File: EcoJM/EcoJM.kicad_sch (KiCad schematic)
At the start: 50 parts, among them J1 Conn_01x01_Pin, J10 Conn_01x01_Pin, J11 Conn_01x01_Pin, J2 Conn_01x01_Pin, J3 Conn_01x02_Pin, J4 Conn_01x02_Pin, J5 Conn_01x03_Pin, J6 Conn_01x02_Pin, J7 Conn_01x03_Pin, J8 Screw_Terminal_01x02, J9 Screw_Terminal_01x02, Q1 2SD882_C842818, Q2 2SD882_C842818, U1 ACS712xLCTR-30A, U2 MT2492, U3 SIT65HVD230DR, U4 AZ1117-3.3, U5 RS321BXF, U6 STM32F_dev, U7 PC817C_C3025164, U8 PC817C_C3025164

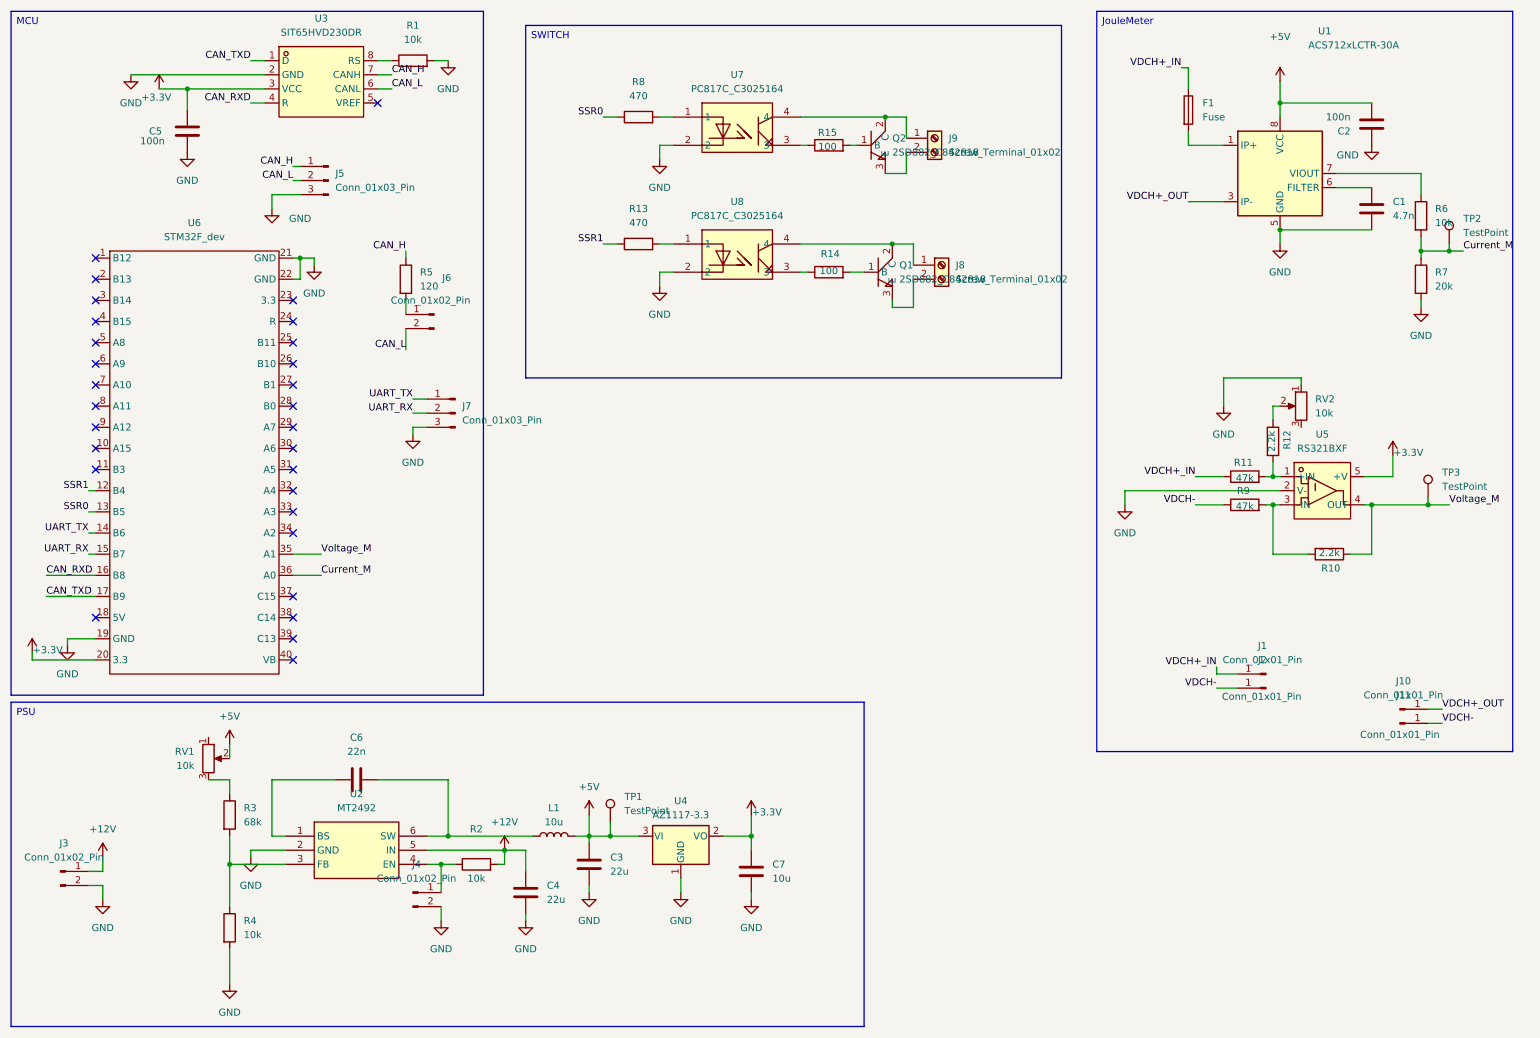
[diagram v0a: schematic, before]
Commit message: diff amp removed + potentiometer removed +SD card schematic done
diff amp removed + potentiometer removed +SD card schematic done
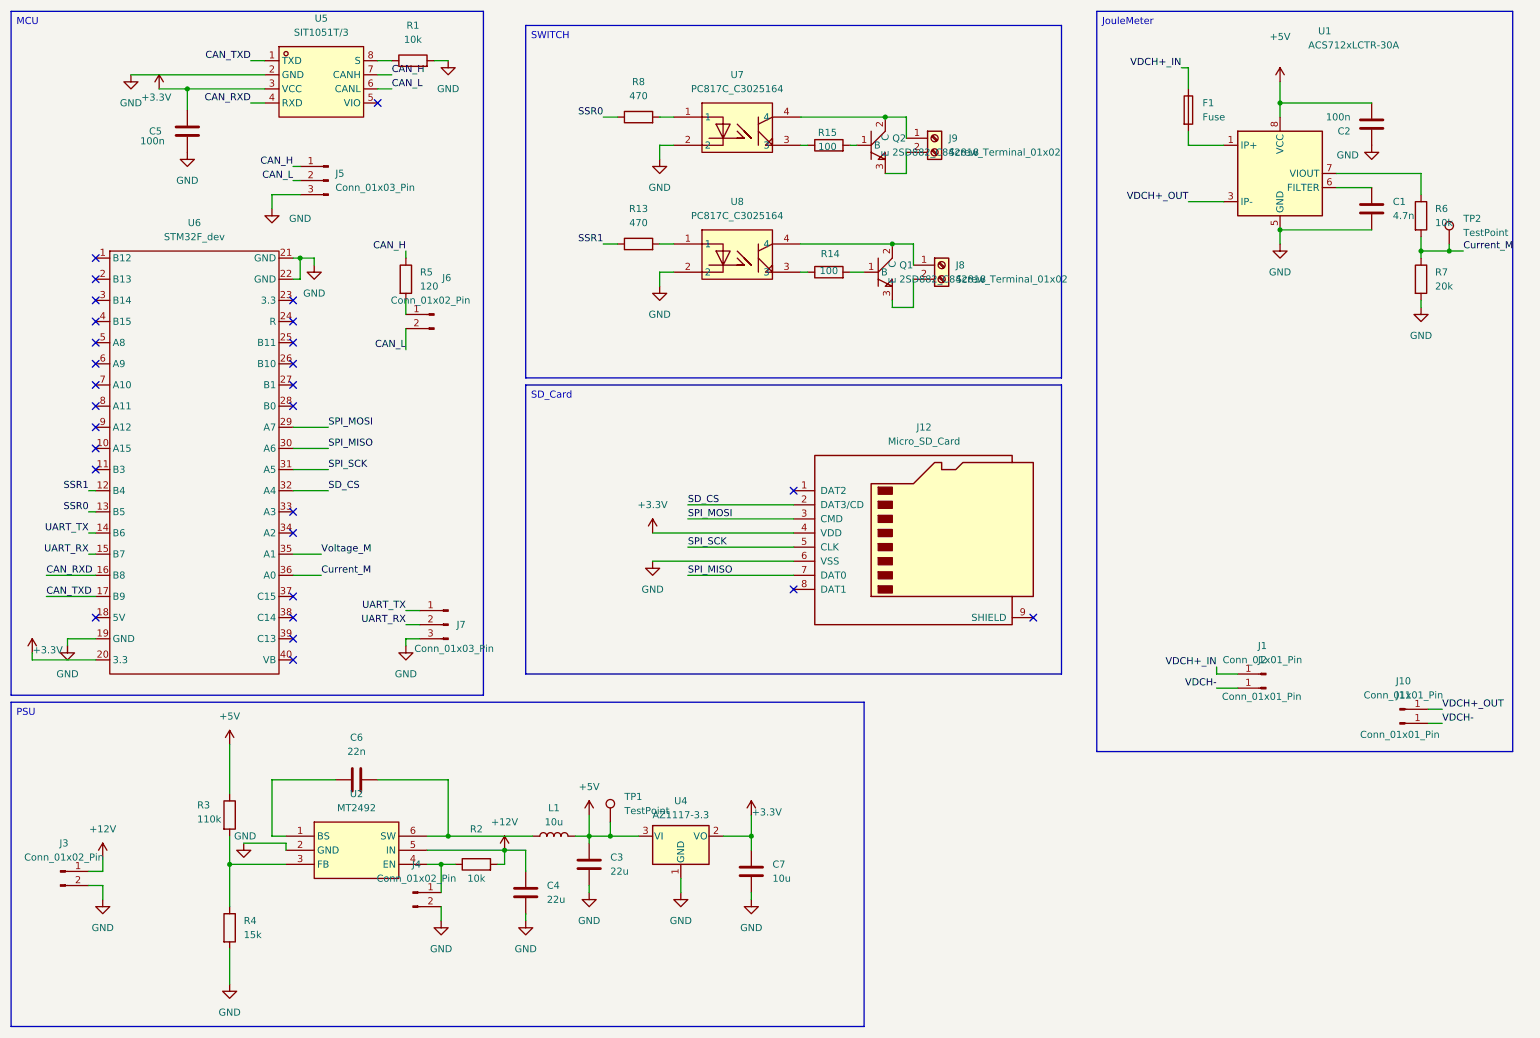
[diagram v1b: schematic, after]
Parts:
- removed R10, R12: 2.2k, Resistor_SMD:R_1206_3216Metric_Pad1.30x1.75mm_HandSolder, symbol Device:R
- removed R11, R9: 47k, Resistor_SMD:R_1206_3216Metric_Pad1.30x1.75mm_HandSolder, symbol Device:R
- removed RV1, RV2: 10k, Potentiometer_THT:Potentiometer_Bourns_3296W_Vertical, symbol Device:R_Potentiometer
- removed TP3: TestPoint, TestPoint:TestPoint_Pad_D1.5mm, symbol Connector:TestPoint
- removed U3: SIT65HVD230DR, EasyEDA:SOP-8_L4.9-W3.9-P1.27-LS6.0-BL, symbol EasyEDA:SIT65HVD230DR
- removed U5: RS321BXF, EasyEDA:SOT-23-5_L2.9-W1.6-P0.95-LS2.8-BL, symbol EasyEDA:RS321BXF
- added J12: Micro_SD_Card, symbol Connector:Micro_SD_Card
- added U5: SIT1051T/3, EasyEDA:SOP-8_L4.9-W3.9-P1.27-LS6.0-BL, symbol EasyEDAA:SIT1051T_3
- R3: value 68k -> 110k
- R4: value 10k -> 15k
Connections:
- net +3.3V: now also J12.4 (VDD), U5.3 (VCC)
- net +5V: now also R3.1
- net CAN_H: now also U5.7 (CANH)
- net CAN_L: now also U5.6 (CANL)
- net CAN_RXD: now also U5.4 (RXD)
- net CAN_TXD: now also U5.1 (TXD)
- net GND: now also J12.6 (VSS), U5.2 (GND)
- net at R1.1: now also U5.8 (S)
- net SPI_MOSI: now reaches U6.29 (A7)
- net SPI_MOSI: now also J12.3 (CMD)
- net SPI_MISO: now reaches U6.30 (A6)
- net SPI_MISO: now also J12.7 (DAT0)
- net SPI_SCK: now reaches U6.31 (A5)
- net SPI_SCK: now also J12.5 (CLK)
- net SD_CS: now reaches U6.32 (A4)
- net SD_CS: now also J12.2 (DAT3/CD)
- no-connect marks 29 -> 28
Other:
- moved on the sheet: J7
